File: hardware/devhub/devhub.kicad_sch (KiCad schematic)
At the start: 0 parts

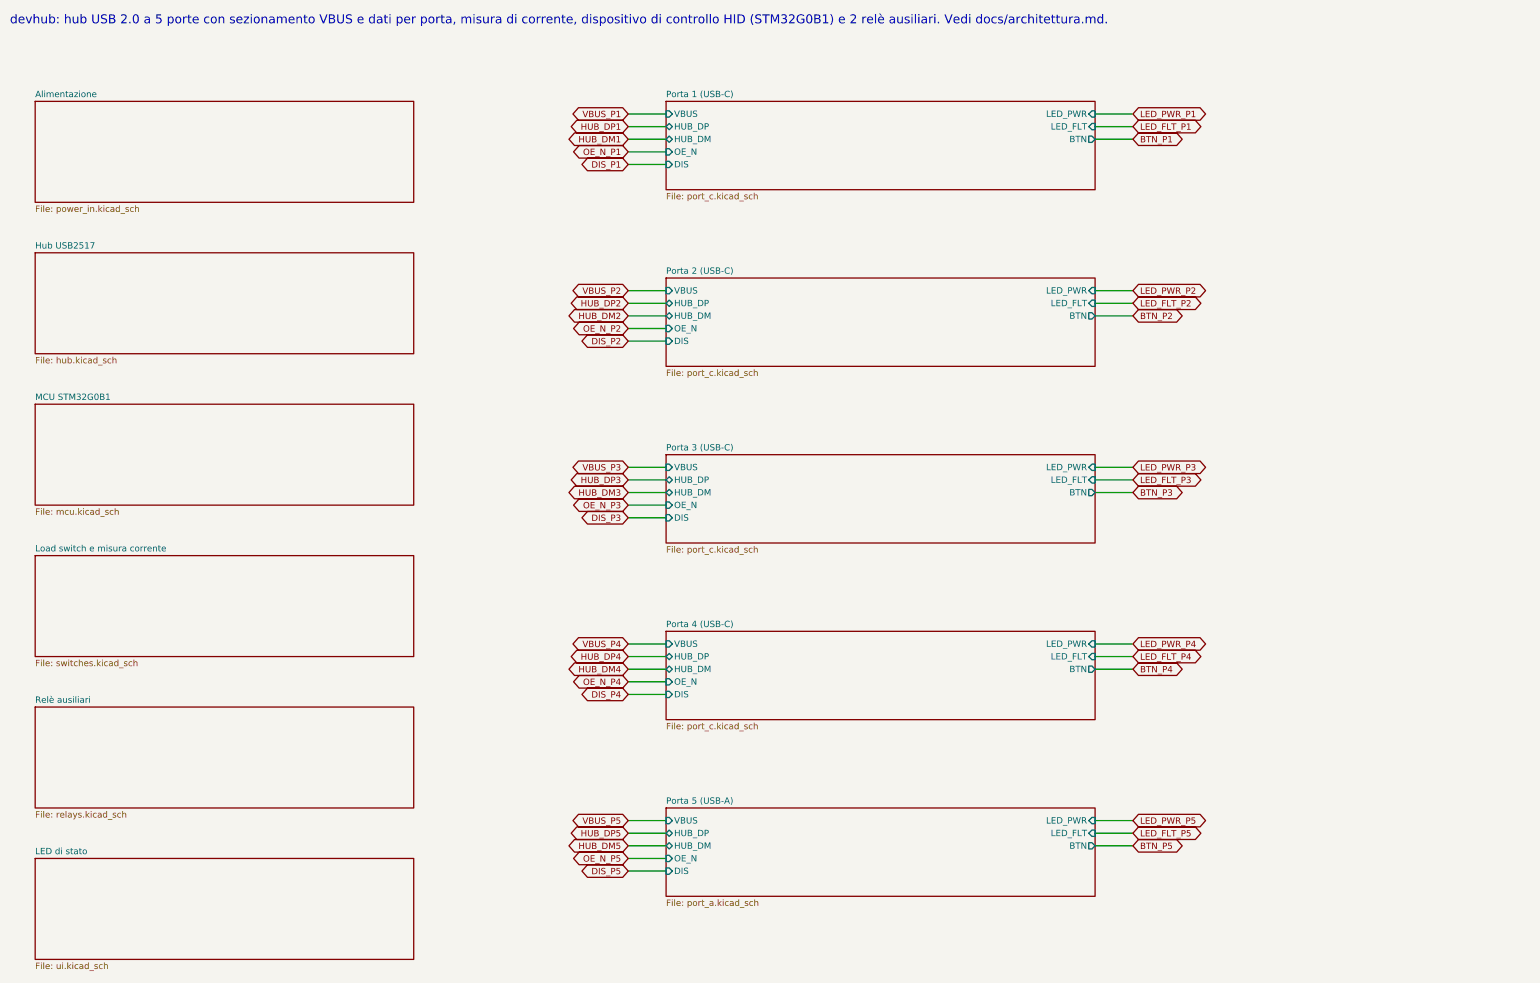
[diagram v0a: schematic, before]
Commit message: Schematic v0.2: hub reset supervisor, 1 A LDO, reorganized sheets, USB connectors and crystal
Functional changes:
- USB2517 RESET_N with pull-up and MCP120T-300 supervisor, wired-OR with
  the MCU (open-drain): resetting the MCU no longer resets the hub, so the
  ST DFU bootloader is reachable through it (D16/D17).
- 3.3 V LDO: AP7361C-33E (1 A, SOT-223) instead of AP2112K, which
  dissipated too much with the hub load.
- 74HC595 /OE on PB6 with pull-up: LEDs off until firmware enables them.
- Orange D93 instead of blue, USB-A bulk capacitance >= 120 uF, relay coil
  pinout fixed, snubbers marked DNP, Cliff FCR7350 banana jack footprints.
- D18: horizontal USB connectors, GCT USB4105-GF-A (USB-C) and Kycon
  KUSBX-AS1N-B (USB-A).
- D19: YXC X322524MOB4SI 24 MHz crystal (C_L 12 pF), 15 pF C0G load caps.

Layout: nearby parts wired directly, every net still explicitly named;
local labels inside sheets, global only across sheets, hierarchical for
ports. Files saved with KiCad 10.

Connectivity checked against the previous netlist, ERC clean.
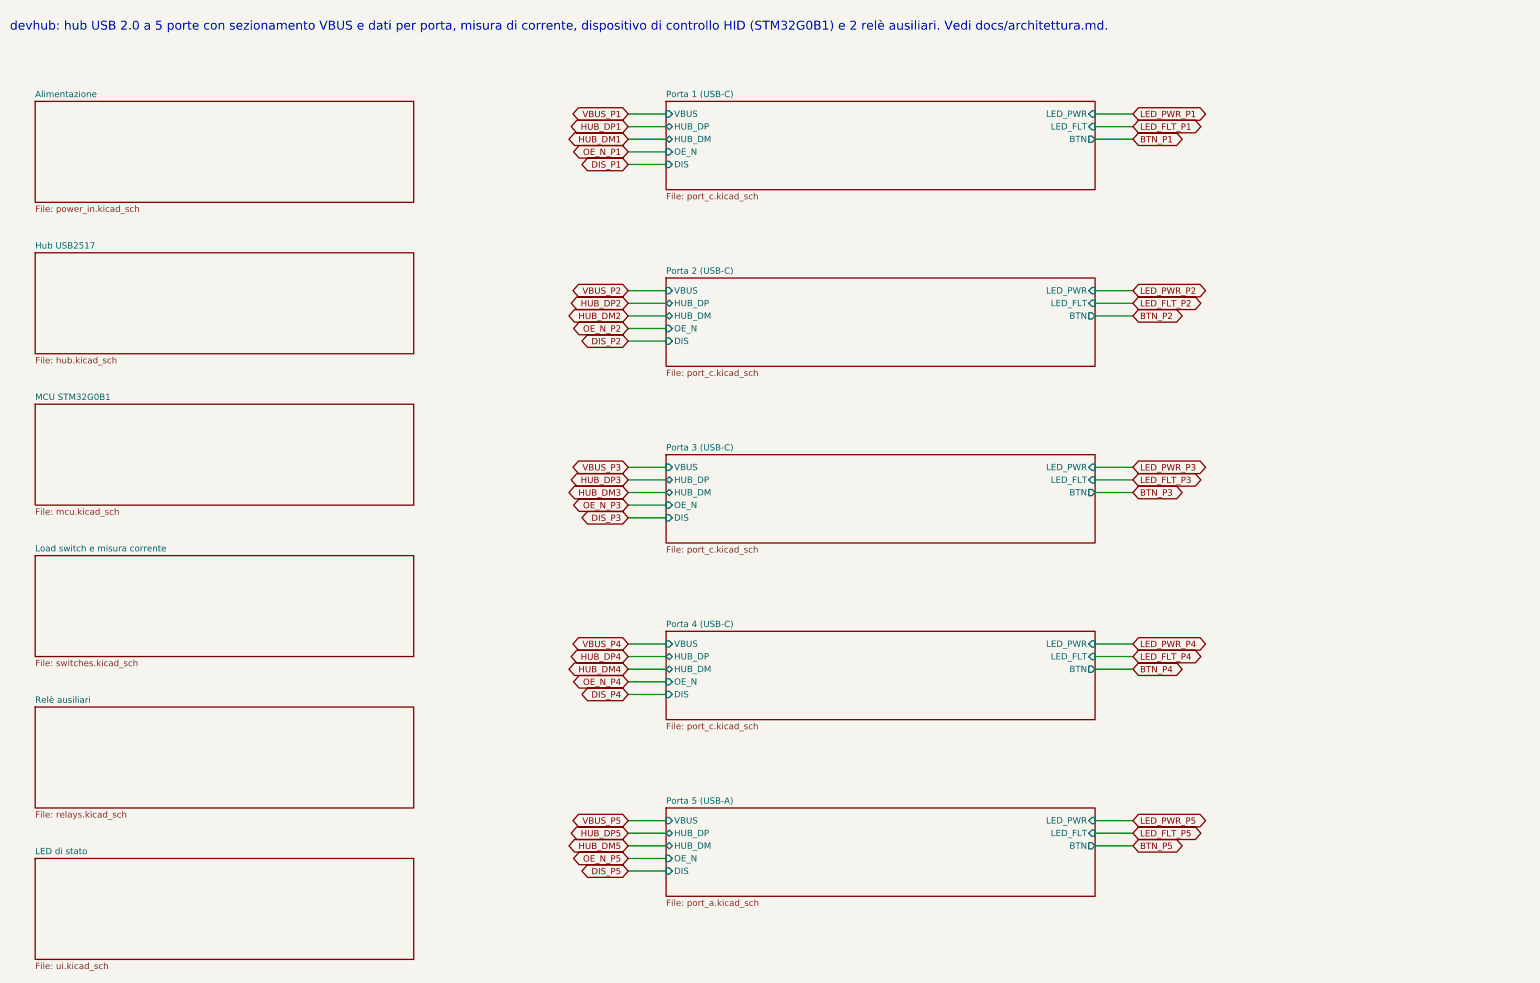
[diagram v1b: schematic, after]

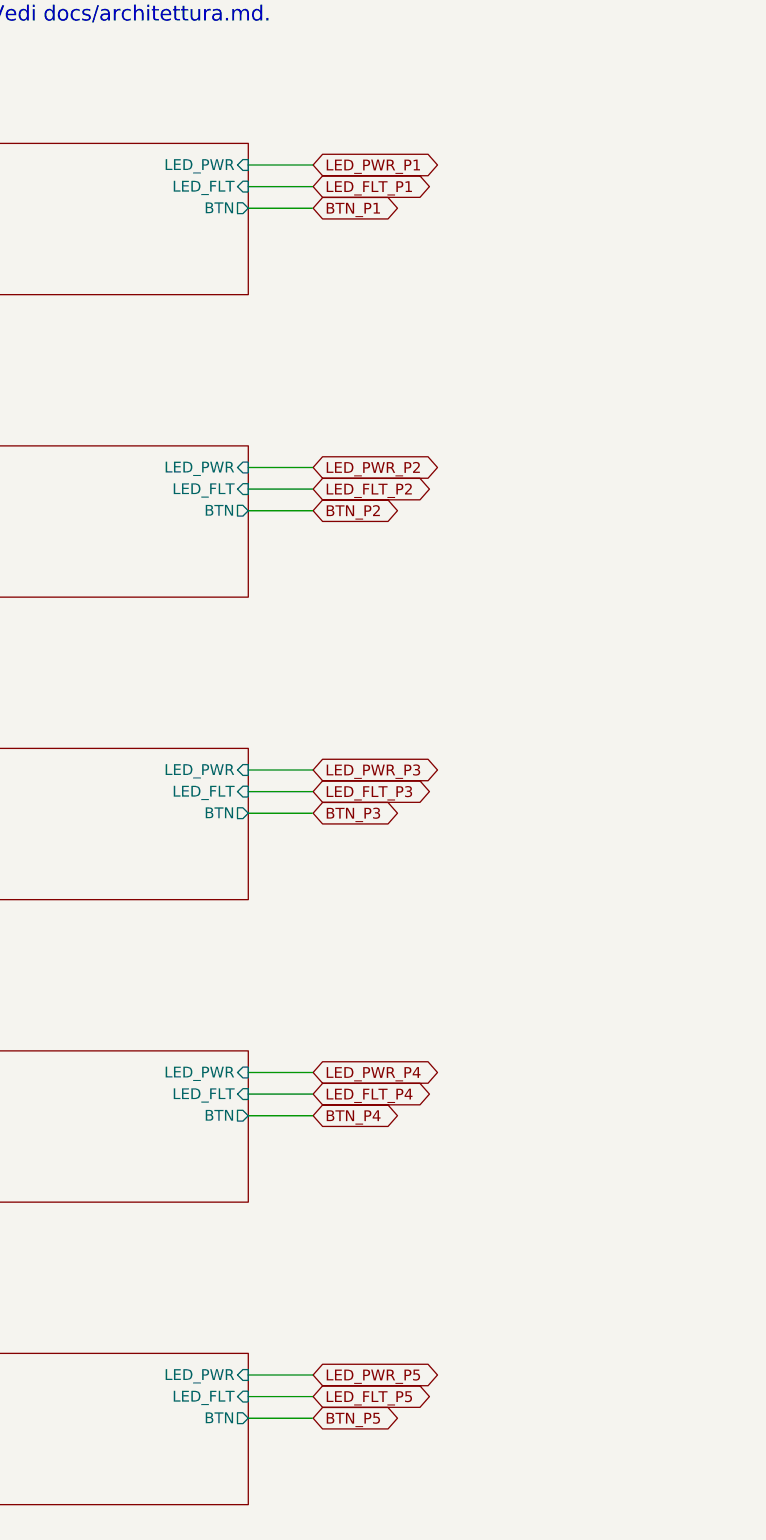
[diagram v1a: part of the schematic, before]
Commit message: Simplification: drop the 74HC595s, green LEDs on port EN, relay LEDs on relay commands (D38)
Red port LEDs and the host LED are driven by GPIOs that stay low in DFU; the power LED is on 3.3 V.
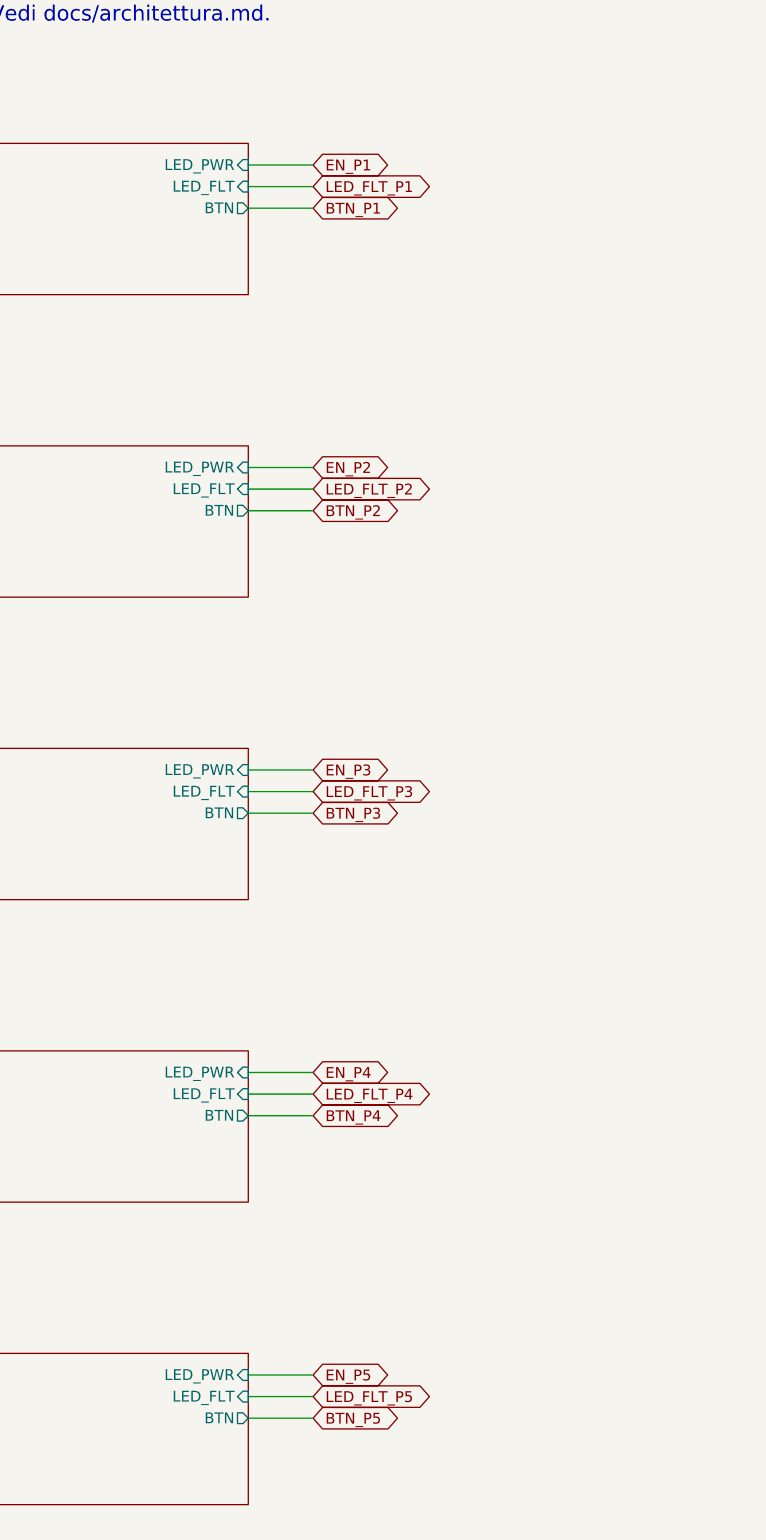
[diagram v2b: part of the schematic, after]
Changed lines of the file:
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@@
 		)
 	)
-	(global_label "LED_PWR_P4"
+	(global_label "EN_P4"
 		(shape bidirectional)
 		(at 236.22 139.7 0)
@@
 		)
 	)
-	(global_label "LED_PWR_P5"
+	(global_label "EN_P5"
 		(shape bidirectional)
 		(at 236.22 175.26 0)
@@
 		)
 	)
-	(global_label "LED_PWR_P3"
+	(global_label "EN_P3"
 		(shape bidirectional)
 		(at 236.22 104.14 0)
@@
 		)
 	)
-	(global_label "LED_PWR_P1"
+	(global_label "EN_P1"
 		(shape bidirectional)
 		(at 236.22 33.02 0)
@@
 		)
 	)
-	(global_label "LED_PWR_P2"
+	(global_label "EN_P2"
 		(shape bidirectional)
 		(at 236.22 68.58 0)

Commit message: PCB rules in KiCad, USB pair names, eFuse output bypass and U2 thermal vias (D44-D50)
Stackup JLC04161H-7628, netclasses and custom DRC rules (devhub.kicad_dru) from
docs/regole-pcb.md, with a section for the checks that DRC cannot cover. C7 1 uF on
the TPS259470A output before the shunt (D48). USB nets renamed to DP/DN so KiCad
recognizes the differential pairs (D49). U2 footprint with 0.3 mm thermal vias, open
on both sides for the prototype; encroached vias and a JLCPCB order note for
production (D50). Also includes stock part codes, cost comparison and placement rules
(D44-D47).
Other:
- sheet Porta 1 (USB-C) ports: added HUB_DN; removed HUB_DM
- sheet Porta 2 (USB-C) ports: added HUB_DN; removed HUB_DM
- sheet Porta 3 (USB-C) ports: added HUB_DN; removed HUB_DM
- sheet Porta 4 (USB-C) ports: added HUB_DN; removed HUB_DM
- sheet Porta 5 (USB-A) ports: added HUB_DN; removed HUB_DM
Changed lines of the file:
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@@
 		)
 	)
-	(global_label "HUB_DM5"
+	(global_label "HUB_DN5"
 		(shape bidirectional)
 		(at 134.62 180.34 180)
@@
 		)
 	)
-	(global_label "HUB_DM3"
+	(global_label "HUB_DN3"
 		(shape bidirectional)
 		(at 134.62 109.22 180)
@@
 		)
 	)
-	(global_label "HUB_DM4"
+	(global_label "HUB_DN4"
 		(shape bidirectional)
 		(at 134.62 144.78 180)
@@
 		)
 	)
-	(global_label "HUB_DM1"
+	(global_label "HUB_DN1"
 		(shape bidirectional)
 		(at 134.62 38.1 180)
@@
 		)
 	)
-	(global_label "HUB_DM2"
+	(global_label "HUB_DN2"
 		(shape bidirectional)
 		(at 134.62 73.66 180)
@@
 			)
 		)
-		(pin "HUB_DM" bidirectional
+		(pin "HUB_DN" bidirectional
 			(at 142.24 180.34 180)
 			(effects
@@
 			)
 		)
-		(pin "HUB_DM" bidirectional
+		(pin "HUB_DN" bidirectional
 			(at 142.24 38.1 180)
 			(effects
@@
 			)
 		)
-		(pin "HUB_DM" bidirectional
+		(pin "HUB_DN" bidirectional
 			(at 142.24 144.78 180)
 			(effects
@@
 			)
 		)
-		(pin "HUB_DM" bidirectional
+		(pin "HUB_DN" bidirectional
 			(at 142.24 73.66 180)
 			(effects
@@
 			)
 		)
-		(pin "HUB_DM" bidirectional
+		(pin "HUB_DN" bidirectional
 			(at 142.24 109.22 180)
 			(effects

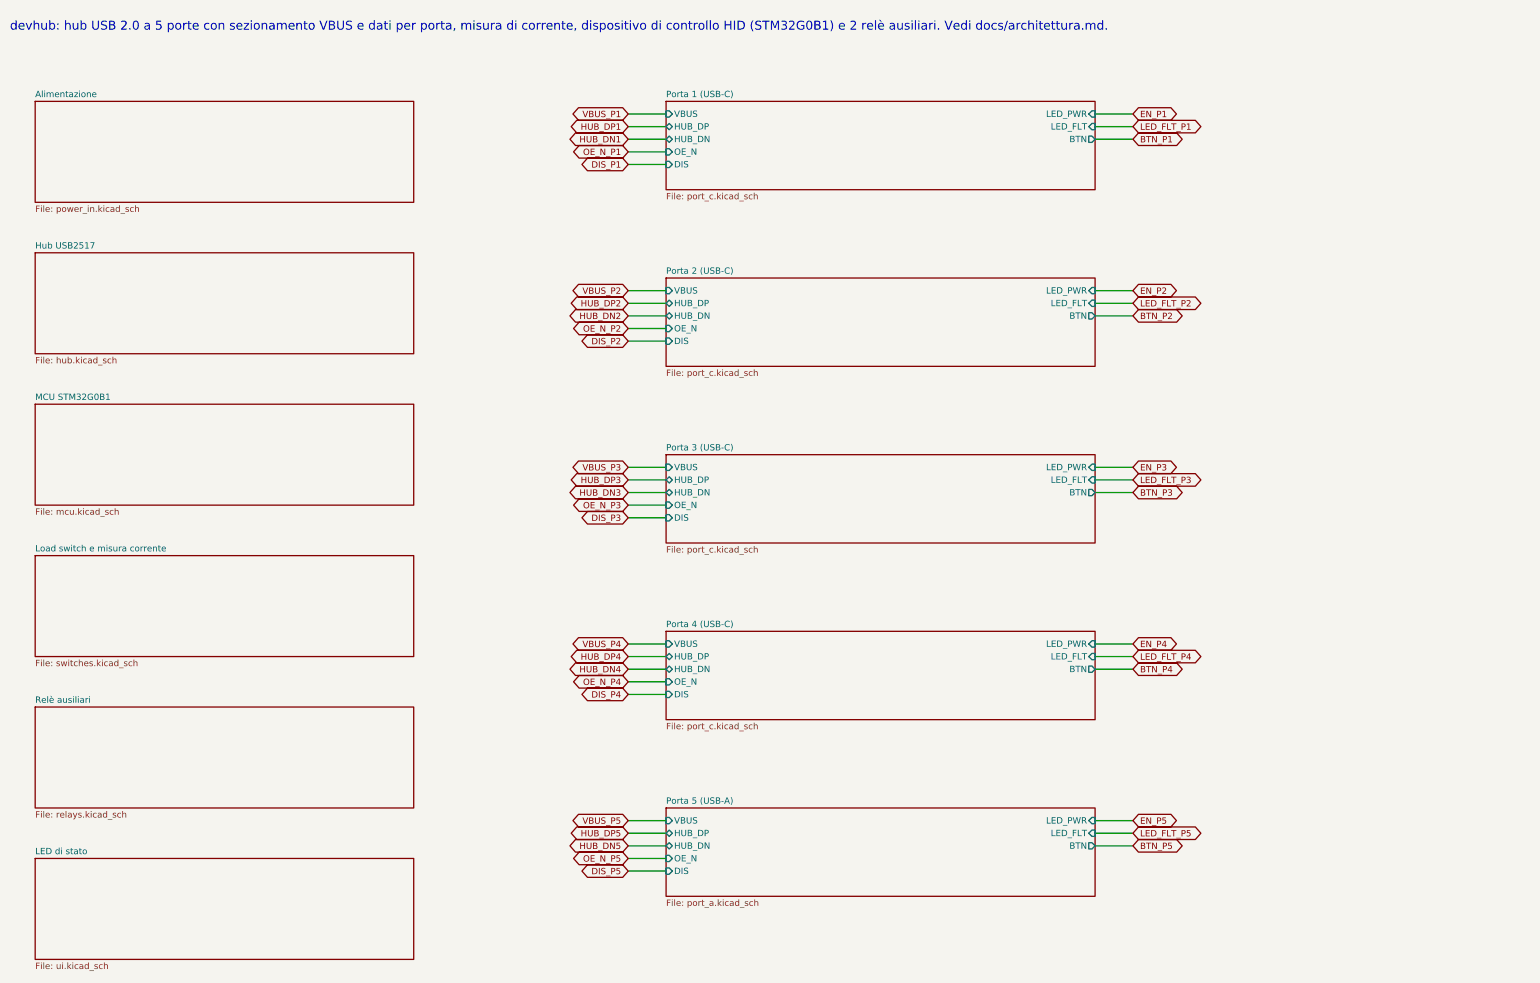
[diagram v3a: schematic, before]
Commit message: Schematic v0.3: apply simplified requirements (D79-D81)
Update the existing KiCad project instead of starting over:
- MCU U3 replaced with STM32G0B1CEU6 (UFQFPN48) on the 48-pin pinout
- switches sheet: two UCS2114-1-V/LX on separate I2C buses replace
  TPS2561A, INA3221 and current shunts
- ports: single MCU-driven LED, discrete VBUS discharge removed
- remove USB-A port, spare hub header, second relay channel,
  input CC ADC filters and input shunt
- add UCS2114 symbol and footprint (Microchip land pattern C04-2421)
- align pinout, decisions, architecture and component docs
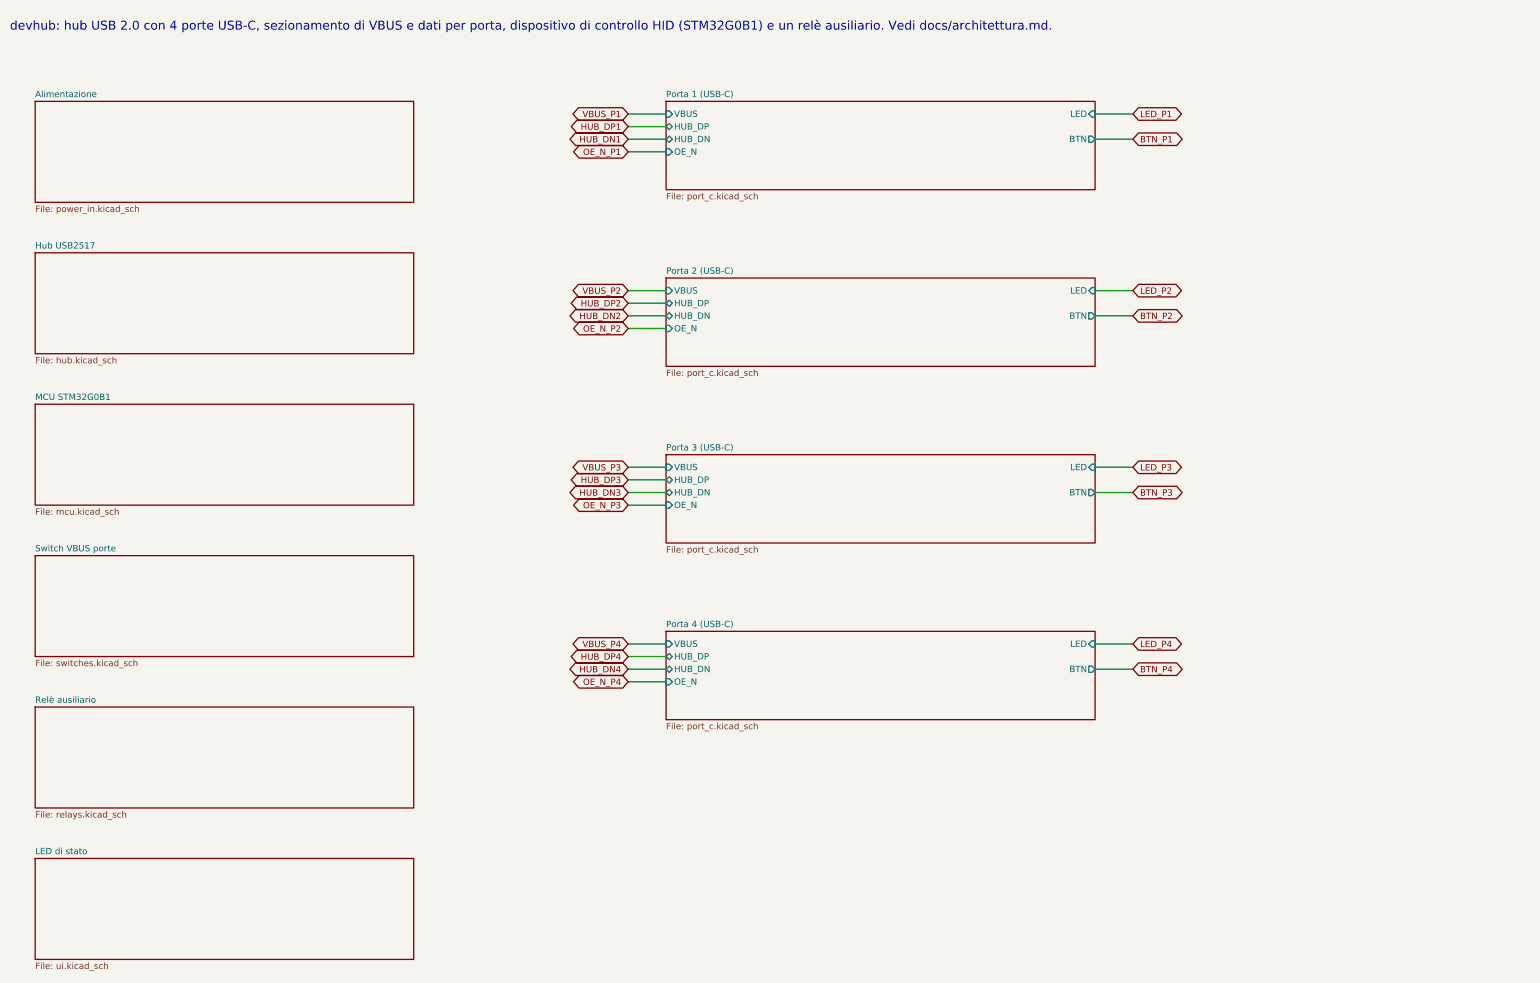
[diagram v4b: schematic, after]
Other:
- sheet Load switch e misura corrente renamed Switch VBUS porte
- sheet Relè ausiliari renamed Relè ausiliario
- removed sheet Porta 5 (USB-A)
- sheet Porta 1 (USB-C) ports: added LED; removed DIS, LED_FLT, LED_PWR
- sheet Porta 2 (USB-C) ports: added LED; removed DIS, LED_FLT, LED_PWR
- sheet Porta 3 (USB-C) ports: added LED; removed DIS, LED_FLT, LED_PWR
- sheet Porta 4 (USB-C) ports: added LED; removed DIS, LED_FLT, LED_PWR
- note added: "devhub: hub USB 2.0 con 4 porte USB-C, sezionamento di VBUS e dati per porta, dispositivo di controllo HID (STM32G0B1) e un relè ausiliario. Vedi docs/architettura.md."
- note removed: "devhub: hub USB 2.0 a 5 porte con sezionamento VBUS e dati per porta, misura di corrente, dispositivo di controllo HID (STM32G0B1) e 2 relè ausiliari. Vedi docs/architettura.md."
